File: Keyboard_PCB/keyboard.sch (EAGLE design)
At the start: 262 parts, among them J1 1-2295018-2, M2 KEYSWITCH-RGBSMDLED-ALPSMX-1U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, M3 KEYSWITCH-RGBSMDLED-ALPSMX-1U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, M4 KEYSWITCH-RGBSMDLED-ALPSMX-1U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, M5 KEYSWITCH-RGBSMDLED-ALPSMX-1U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, M6 KEYSWITCH-RGBSMDLED-ALPSMX-1U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, Y2 CRYSTAL-GROUNDEDSMD-3.2X2.5

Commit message: Thing
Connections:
- removed net COL1: CTRL1.P0, M2.P0, M3.P0, M4.P0, M5.P0, M6.P0
- removed net N$239: J1.VBUS@2
- new net COL11: 8.P0, COMMA.P0, F8.P0, I.P0, IC3.PC5_A13_OC3B, K.P0
- new net N$102: CTRL.P1, DCTRL.A
- net +5V: now also 0.VCC, 1.VCC, 2.VCC, 3.VCC, 4.VCC, 5.VCC, 6.VCC, 7.VCC, 8.VCC, 9.VCC, A.VCC, ALT.VCC, ALT2.VCC, B.VCC, BACKSONG.VCC, BACKSPACE_1.VCC, C.VCC, CAPSLOCK.VCC, COMMA.VCC, CTRL.VCC, CTRL1.VCC, D.VCC, DASH.VCC, DELETE.VCC, DOWN.VCC, E.VCC, END.VCC, ENTER2.VCC, EQUAL.VCC, ESC.VCC, F.VCC, F1.VCC, F10.VCC, F11.VCC, F12.VCC, F2.VCC, F3.VCC, F4.VCC, F5.VCC, F6.VCC, F7.VCC, F9.VCC, G.VCC, GRAVE.VCC, H.VCC, HOME.VCC, I.VCC, INSERT.VCC, J.VCC, J1.VBUS@2, K.VCC, KP_0.VCC, KP_1.VCC, KP_3.VCC, KP_4.VCC, KP_5.VCC, KP_6.VCC, KP_62.VCC, KP_7.VCC, KP_9.VCC, KP_ASTERISK.VCC, KP_DASH.VCC, KP_DEL.VCC, KP_DELETE2.VCC, L.VCC, LBRACKET.VCC, LEFT.VCC, LOCK.VCC, M.VCC, M2.VCC, M3.VCC, M4.VCC, M5.VCC, M6.VCC, MENU.VCC, N.VCC, NEXTSONG.VCC, NUMLOCK.VCC, O.VCC, P.VCC, PAUSE.VCC, PAUSEPLAY.VCC, PERIOD.VCC, PGDN.VCC, PGUP.VCC, PLUS2.VCC, PRTSC.VCC, Q.VCC, QUOTE.VCC, R.VCC, RANDSONG.VCC, RBRACKET.VCC, RIGHT.VCC, S.VCC, SCROLLLOCK.VCC, SEMICOLON.VCC, SHIFT.VCC, SLASH.VCC, SPACE.VCC, T.VCC, TAB.VCC, U.VCC, UNDERSCORE.VCC, UP.VCC, V.VCC, VOLUMEUP.VCC, W.VCC, WIN.VCC, WIN2.VCC, X.VCC, Y.VCC, Z.VCC
- net COL10: now also 7.P0, F7.P0, IC3.PC6_A14_OC3A, J.P0, M.P0, U.P0; no longer 8.P0, COMMA.P0, F8.P0, I.P0, K.P0
- net COL12: now also IC3.PC4_A12_OC3C
- net COL13: now also IC3.PC3_A11_T3
- net COL14: now also IC3.PC2_A10
- net COL15: now also IC3.PC1_A9
- net COL16: now also IC3.PC0_A8
- net COL17: now also IC3.PE1_/RD
- net COL18: now also IC3.PE0_/WR
- net COL19: now also IC3.PD7_T0
- net COL2: now also CTRL1.P0, IC3.PA1_AD1, M2.P0, M3.P0, M4.P0, M5.P0, M6.P0; no longer CAPSLOCK.P0, CTRL.P0, ESC.P0, GRAVE.P0, SHIFT.P0, TAB.P0
- net COL20: now also IC3.PD6_T1
- net COL21: now also IC3.PD5_XCK1
- net COL22: now also IC3.PD4_ICP1
- net COL23: now also IC3.PD3_TXD1_INT3
- net COL24: now also IC3.PD2_RXD1_INT2
- net COL25: now also IC3.PD1_OC2B_SDA_INT1
- net COL3: now also CAPSLOCK.P0, CTRL.P0, ESC.P0, GRAVE.P0, IC3.PA2_AD2, SHIFT.P0, TAB.P0; no longer 1.P0, A.P0, F1.P0, Q.P0, WIN.P0, Z.P0
- net COL4: now also 1.P0, A.P0, F1.P0, IC3.PA3_AD3, Q.P0, WIN.P0, Z.P0; no longer 2.P0, ALT.P0, F2.P0, S.P0, W.P0, X.P0
- net COL5: now also 2.P0, ALT.P0, F2.P0, IC3.PA4_AD4, S.P0, W.P0, X.P0; no longer 3.P0, C.P0, D.P0, E.P0, F3.P0
- net COL6: now also 3.P0, C.P0, D.P0, E.P0, F3.P0, IC3.PA5_AD5; no longer 4.P0, F.P0, F4.P0, R.P0, V.P0
- net COL7: now also 4.P0, F.P0, F4.P0, IC3.PA6_AD6, R.P0, V.P0; no longer 5.P0, B.P0, F5.P0, G.P0, SPACE.P0, T.P0
- net COL8: now also 5.P0, B.P0, F5.P0, G.P0, IC3.PA7_AD7, SPACE.P0, T.P0; no longer 6.P0, F6.P0, H.P0, N.P0, Y.P0
- net COL9: now also 6.P0, F6.P0, H.P0, IC3.PC7_A15_IC3_CLK0, N.P0, Y.P0; no longer 7.P0, F7.P0, J.P0, M.P0, U.P0
- net GND: now also 0.GND, 1.GND, 2.GND, 3.GND, 4.GND, 5.GND, 6.GND, 7.GND, 8.GND, 9.GND, A.GND, ALT.GND, ALT2.GND, B.GND, BACKSLASH.GND, BACKSONG.GND, BACKSPACE.GND, BACKSPACE_1.GND, C.GND, CAPSLOCK.GND, COMMA.GND, CTRL.GND, CTRL1.GND, CTRL2.GND, D.GND, DASH.GND, DELETE.GND, DOWN.GND, E.GND, END.GND, ENTER.GND, ENTER2.GND, EQUAL.GND, ESC.GND, F.GND, F1.GND, F10.GND, F11.GND, F12.GND, F2.GND, F3.GND, F4.GND, F5.GND, F6.GND, F7.GND, F8.GND, F9.GND, G.GND, GRAVE.GND, H.GND, HOME.GND, I.GND, INSERT.GND, J.GND, K.GND, KP_0.GND, KP_1.GND, KP_2.GND, KP_3.GND, KP_4.GND, KP_5.GND, KP_52.GND, KP_6.GND, KP_62.GND, KP_7.GND, KP_8.GND, KP_9.GND, KP_ASTERISK.GND, KP_DASH.GND, KP_DEL.GND, KP_DELETE2.GND, KP_SLASH.GND, L.GND, LBRACKET.GND, LEFT.GND, LOCK.GND, M.GND, M2.GND, M3.GND, M4.GND, M5.GND, M6.GND, MENU.GND, N.GND, NEXTSONG.GND, NUMLOCK.GND, O.GND, P.GND, PAUSE.GND, PAUSEPLAY.GND, PERIOD.GND, PGDN.GND, PGUP.GND, PLUS2.GND, PRTSC.GND, Q.GND, QUOTE.GND, R.GND, RANDSONG.GND, RBRACKET.GND, RIGHT.GND, S.GND, SCROLLLOCK.GND, SEMICOLON.GND, SHIFT.GND, SHIFT2.GND, SLASH.GND, SPACE.GND, T.GND, TAB.GND, U.GND, UNDERSCORE.GND, UP.GND, V.GND, VOLUMEUP.GND, VOLUMNEDOWN.GND, W.GND, WIN.GND, WIN2.GND, X.GND, Y.GND, Z.GND
- net LED1: now also IC3.PF7_ADC7_TDI
- net LED2: now also IC3.PF6_ADC6_TDO
- net LED3: now also IC3.PF5_ADC5_TMS
- net LED4: now also IC3.PF4_ADC4_TCK
- net LED5: now also IC3.PF3_ADC3
- net LED6: now also IC3.PF2_ADC2
- net ROW1: now also IC3.PB5_PCINT5_OC1A
- net ROW2: now also IC3.PB4_PCINT4_OC2A
- net ROW3: now also IC3.PB3_PDO_PCINT3_MISO
- net ROW4: now also IC3.PB2_PDI_PCINT2_MOSI
- net ROW5: now also IC3.PB1_PCINT1_SCLK
- net ROW6: now also DCTRL.C, IC3.PB0_SS_PCINT0
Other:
- moved on the sheet: BACKSPACE, ENTER, KP_0, SHIFT, SHIFT2

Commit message: Updated keyboard schematic. Slowely making progress
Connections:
- net +5V: now also F8.VCC, VOLUMNEDOWN.VCC
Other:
- moved on the sheet: SPACE
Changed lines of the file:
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@@
 <part name="P+172" library="supply1" library_urn="urn:adsk.eagle:library:371" deviceset="+5V" device=""/>
 <part name="P+174" library="supply1" library_urn="urn:adsk.eagle:library:371" deviceset="+5V" device=""/>
+<part name="P+32" library="supply1" library_urn="urn:adsk.eagle:library:371" deviceset="+5V" device=""/>
 </parts>
 <sheets>
@@
 <instance part="P+172" gate="1" x="906.272" y="-332.74" smashed="yes"/>
 <instance part="P+174" gate="1" x="977.392" y="-332.74" smashed="yes"/>
+<instance part="P+32" gate="1" x="350.52" y="5.08" smashed="yes"/>
 </instances>
 <busses>
@@
 <pinref part="P+23" gate="1" pin="+5V"/>
 <wire x1="570.992" y1="2.54" x2="570.992" y2="0" width="0.1524" layer="91"/>
-<wire x1="570.992" y1="0" x2="567.69" y2="0" width="0.1524" layer="91"/>
+<wire x1="570.992" y1="0" x2="567.563" y2="0" width="0.1524" layer="91"/>
+<pinref part="VOLUMNEDOWN" gate="G$1" pin="VCC"/>
+<wire x1="567.563" y1="0" x2="567.436" y2="0" width="0.1524" layer="91"/>
+<junction x="567.563" y="0"/>
 </segment>
 <segment>
@@
 <pinref part="BACKSPACE_1" gate="G$1" pin="VCC"/>
 </segment>
+<segment>
+<pinref part="P+32" gate="1" pin="+5V"/>
+<wire x1="350.52" y1="2.54" x2="350.52" y2="0" width="0.1524" layer="91"/>
+<wire x1="350.52" y1="0" x2="347.218" y2="0" width="0.1524" layer="91"/>
+<pinref part="F8" gate="G$1" pin="VCC"/>
+</segment>
 </net>

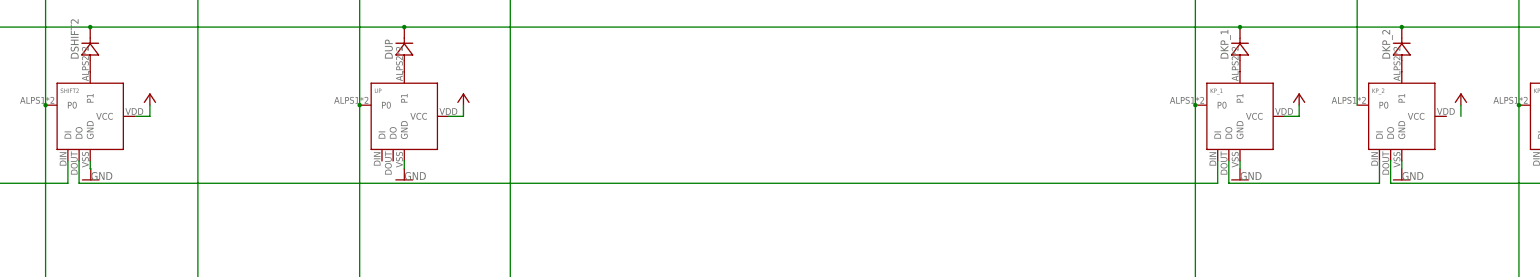
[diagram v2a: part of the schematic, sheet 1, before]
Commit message: Updated before rework of keys
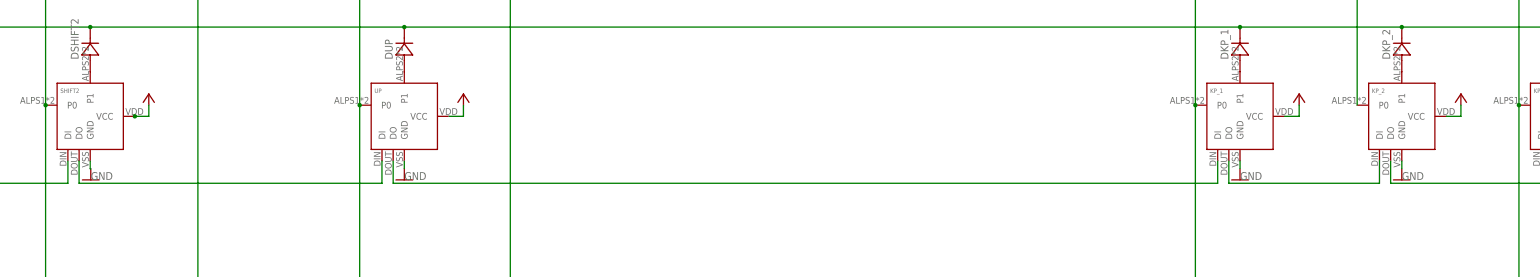
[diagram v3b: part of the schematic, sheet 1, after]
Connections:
- new net N$117: SHIFT2.DO, UP.DI
- net +5V: now also KP_2.VCC, SHIFT2.VCC
- net N$230: now also UP.DO; no longer SHIFT2.DO
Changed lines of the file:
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@@
 <instance part="P+137" gate="1" x="387.35" y="-261.62" smashed="yes"/>
 <instance part="P+138" gate="1" x="424.18" y="-261.62" smashed="yes"/>
-<instance part="P+142" gate="1" x="570.992" y="-261.62" smashed="yes"/>
+<instance part="P+142" gate="1" x="570.738" y="-261.62" smashed="yes"/>
 <instance part="P+144" gate="1" x="642.366" y="-261.62" smashed="yes"/>
 <instance part="P+146" gate="1" x="832.612" y="-261.62" smashed="yes"/>
@@
 <net name="N$230" class="0">
 <segment>
-<wire x1="554.863" y1="-276.86" x2="554.863" y2="-281.94" width="0.1524" layer="91"/>
-<wire x1="554.863" y1="-281.94" x2="814.07" y2="-281.94" width="0.1524" layer="91"/>
-<wire x1="814.07" y1="-281.94" x2="814.07" y2="-276.86" width="0.1524" layer="91"/>
-<pinref part="SHIFT2" gate="G$1" pin="DO"/>
 <pinref part="KP_1" gate="G$1" pin="DI"/>
+<pinref part="UP" gate="G$1" pin="DO"/>
+<wire x1="626.364" y1="-276.86" x2="626.364" y2="-281.94" width="0.1524" layer="91"/>
+<wire x1="626.364" y1="-281.94" x2="814.07" y2="-281.94" width="0.1524" layer="91"/>
+<wire x1="814.07" y1="-281.94" x2="814.07" y2="-276.86" width="0.1524" layer="91"/>
 </segment>
 </net>
@@
 <segment>
 <pinref part="P+142" gate="1" pin="+5V"/>
-<wire x1="570.992" y1="-264.16" x2="570.992" y2="-266.7" width="0.1524" layer="91"/>
-<wire x1="570.992" y1="-266.7" x2="567.69" y2="-266.7" width="0.1524" layer="91"/>
+<wire x1="570.738" y1="-264.16" x2="570.738" y2="-266.7" width="0.1524" layer="91"/>
+<wire x1="570.738" y1="-266.7" x2="567.563" y2="-266.7" width="0.1524" layer="91"/>
+<pinref part="SHIFT2" gate="G$1" pin="VCC"/>
+<wire x1="567.563" y1="-266.7" x2="567.436" y2="-266.7" width="0.1524" layer="91"/>
+<junction x="567.563" y="-266.7"/>
 </segment>
 <segment>
@@
 <pinref part="P+147" gate="1" pin="+5V"/>
 <wire x1="869.442" y1="-264.16" x2="869.442" y2="-266.7" width="0.1524" layer="91"/>
+<pinref part="KP_2" gate="G$1" pin="VCC"/>
+<wire x1="866.14" y1="-266.7" x2="869.442" y2="-266.7" width="0.1524" layer="91"/>
 </segment>
 <segment>
@@
 </segment>
 </net>
+<net name="N$117" class="0">
+<segment>
+<pinref part="SHIFT2" gate="G$1" pin="DO"/>
+<wire x1="554.863" y1="-276.86" x2="554.863" y2="-281.94" width="0.1524" layer="91"/>
+<wire x1="554.863" y1="-281.94" x2="623.824" y2="-281.94" width="0.1524" layer="91"/>
+<pinref part="UP" gate="G$1" pin="DI"/>
+<wire x1="623.824" y1="-281.94" x2="623.824" y2="-276.86" width="0.1524" layer="91"/>
+</segment>
+</net>

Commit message: blank reverse
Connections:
- net LED1: now also IC3.PB5_PCINT5_OC1A; no longer IC3.PF7_ADC7_TDI
- net LED2: now also IC3.PB4_PCINT4_OC2A; no longer IC3.PF6_ADC6_TDO
- net LED3: now also IC3.PB3_PDO_PCINT3_MISO; no longer IC3.PF5_ADC5_TMS
- net LED4: now also IC3.PB2_PDI_PCINT2_MOSI; no longer IC3.PF4_ADC4_TCK
- net LED5: now also IC3.PB1_PCINT1_SCLK; no longer IC3.PF3_ADC3
- net LED6: now also IC3.PB0_SS_PCINT0; no longer IC3.PF2_ADC2
- net ROW1: now also IC3.PF7_ADC7_TDI; no longer IC3.PB5_PCINT5_OC1A
- net ROW2: now also IC3.PF6_ADC6_TDO; no longer IC3.PB4_PCINT4_OC2A
- net ROW3: now also IC3.PF5_ADC5_TMS; no longer IC3.PB3_PDO_PCINT3_MISO
- net ROW4: now also IC3.PF4_ADC4_TCK; no longer IC3.PB2_PDI_PCINT2_MOSI
- net ROW5: now also IC3.PF3_ADC3; no longer IC3.PB1_PCINT1_SCLK
- net ROW6: now also IC3.PF2_ADC2; no longer IC3.PB0_SS_PCINT0
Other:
- moved on the sheet: BACKSPACE, ENTER, ENTER2, KP_0, PLUS2, SHIFT, SHIFT2, SPACE
